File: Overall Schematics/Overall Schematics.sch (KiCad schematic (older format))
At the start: 27 parts, among them U1 Teensy4.1

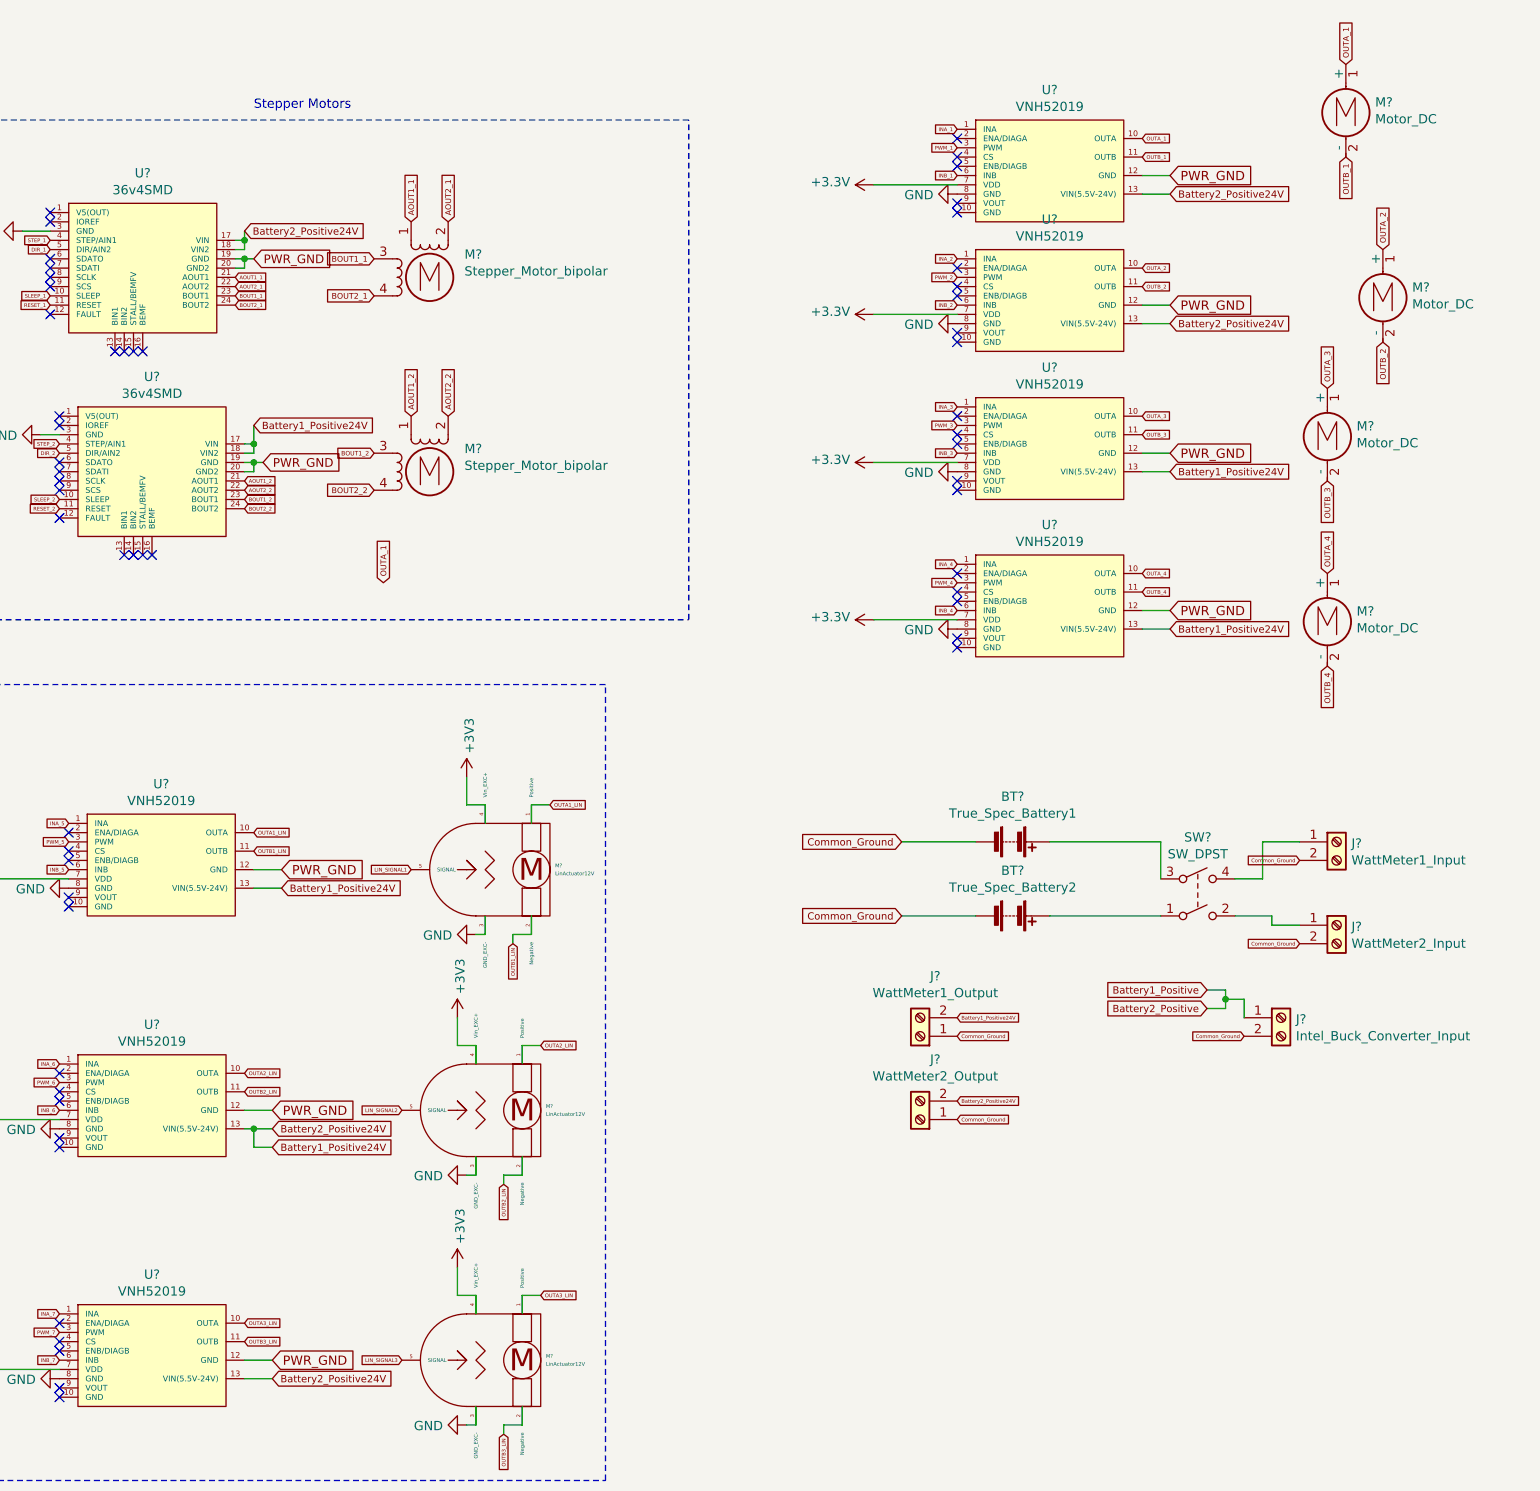
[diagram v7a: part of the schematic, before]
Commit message: motor drive footprints completed (ready for pcb)
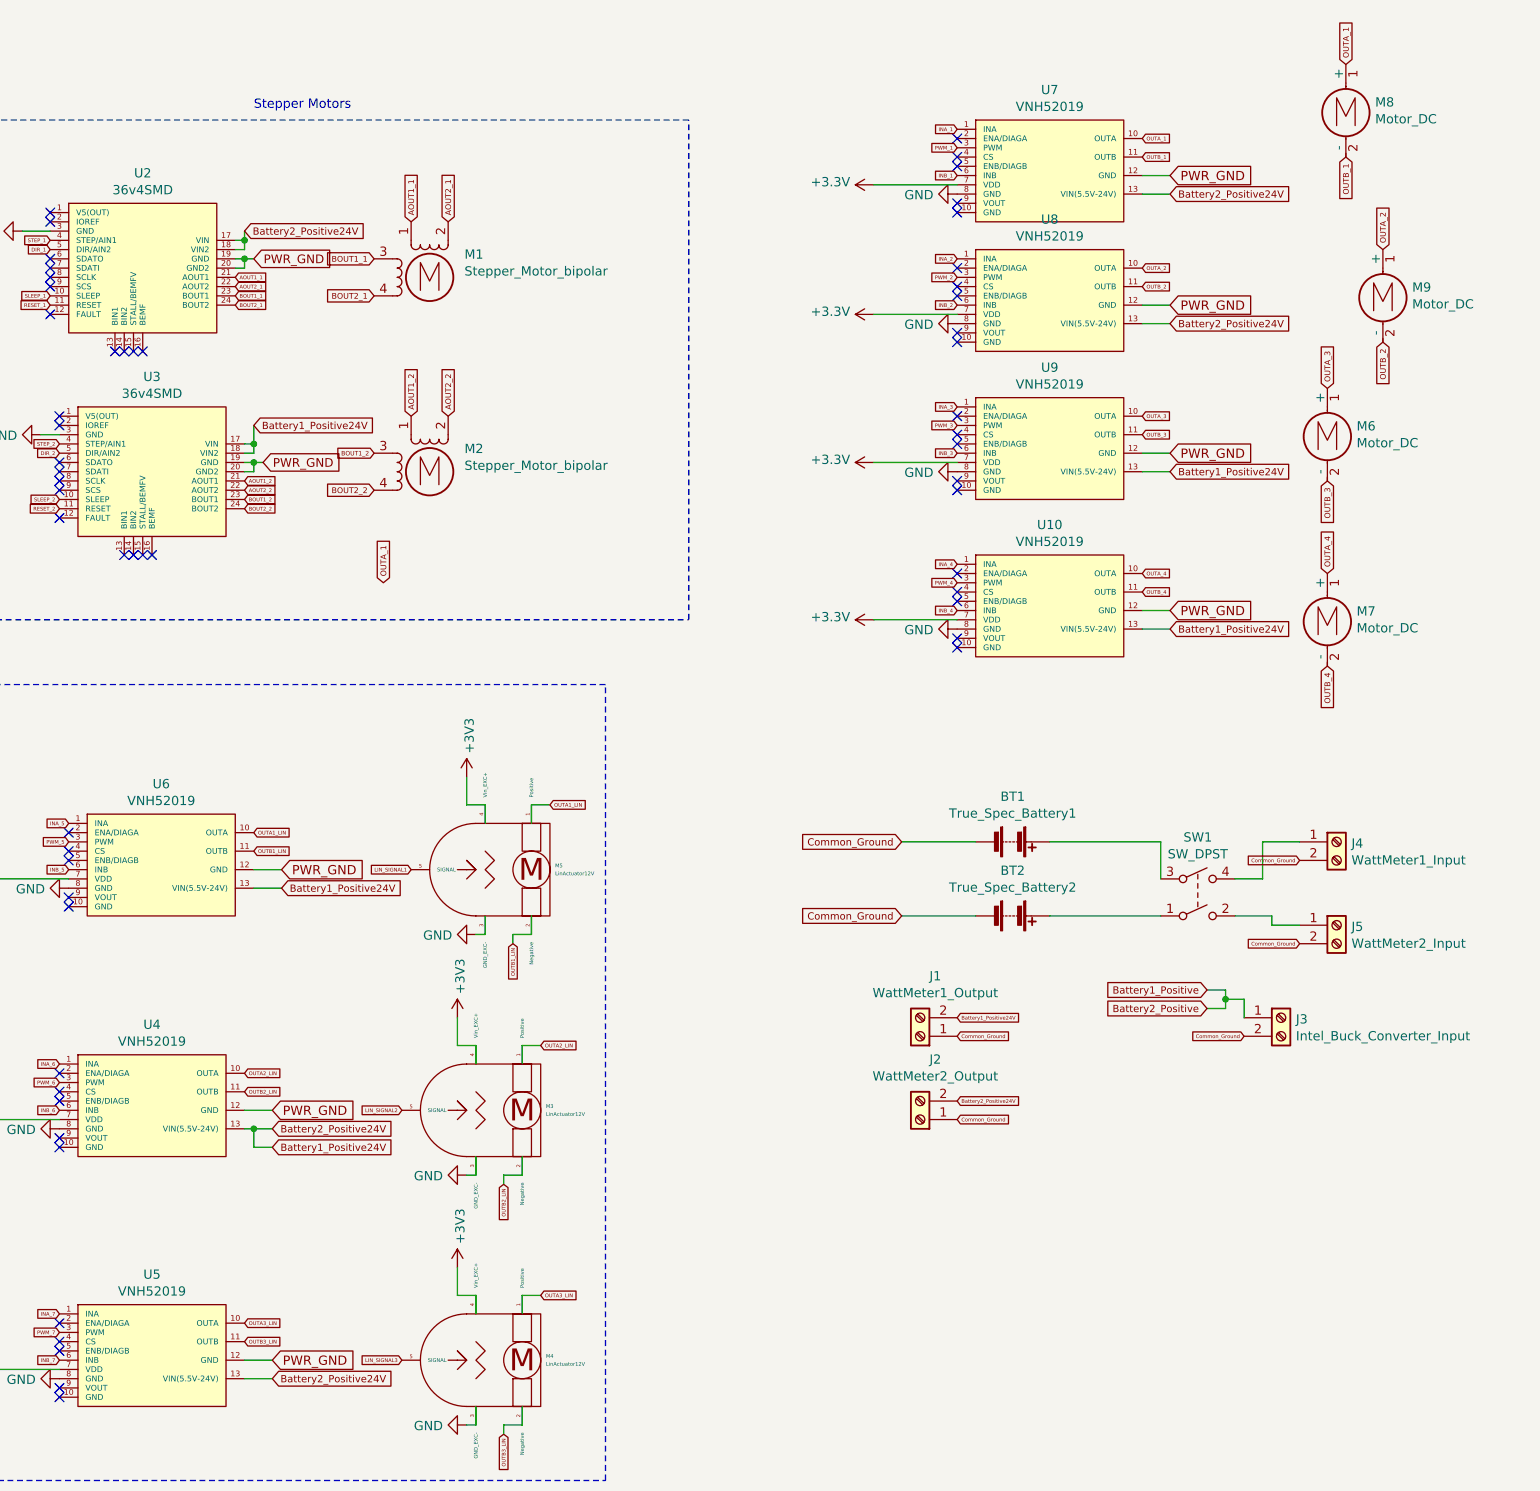
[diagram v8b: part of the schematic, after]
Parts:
- U10, U4, U5, U6, U7, U8, U9: renamed from U?; footprint (none) -> Custom Footprints:DCMotorDriver
- U2, U3: renamed from U?; footprint (none) -> Custom Footprints:StepperMotorDriver
- gave numbers to parts that had none: 17
